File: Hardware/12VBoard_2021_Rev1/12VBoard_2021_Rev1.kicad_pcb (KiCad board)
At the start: 2 copper layers, 178 parts, among them Q1 CSD18537NQ5A, Q2 CSD18531Q5A, Q3 IRFZ34, Q4 CSD18537NQ5A, Q5 CSD18531Q5A, Q6 CSD18537NQ5A, Q7 CSD18531Q5A, SW1 SW_SPDT, U1 LM2576SX-5.0/NOPB, U10 LM5116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

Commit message: fixed H pins x2
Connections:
- net /Tiva In/Outputs/DriveSense renamed Net-(Conn1-Pad1)
- C11 pad 1: /High Current Outputs/Multimedia/Extra/PackVoltage -> /High Current Outputs/PackVoltage
- C14 pad 1: /High Current Outputs/Multimedia/Extra/PackVoltage -> /High Current Outputs/PackVoltage
- C24 pad 1: /High Current Outputs/AuxMount/PackVoltage -> /High Current Outputs/PackVoltage
- C26 pad 1: /High Current Outputs/AuxMount/PackVoltage -> /High Current Outputs/PackVoltage
- C46 pad 1: /High Current Outputs/Multimedia/Extra/PackVoltage -> /High Current Outputs/PackVoltage
- C50 pad 1: /High Current Outputs/AuxMount/PackVoltage -> /High Current Outputs/PackVoltage
- Conn1 pad 3: /Tiva In/Outputs/MulitmediaSense -> /High Current Outputs/MultimediaSense
- R20 pad 1: /High Current Outputs/AuxMount/PackVoltage -> /High Current Outputs/PackVoltage
- R9 pad 1: /High Current Outputs/Multimedia/Extra/PackVoltage -> /High Current Outputs/PackVoltage
- U10 pad 1: /High Current Outputs/AuxMount/PackVoltage -> /High Current Outputs/PackVoltage
- U15 pad 1: /High Current Outputs/Multimedia/Extra/PackVoltage -> /High Current Outputs/PackVoltage
- U17 pad 1: /High Current Outputs/AuxMount/PackVoltage -> /High Current Outputs/PackVoltage
- U7 pad 1: /High Current Outputs/Multimedia/Extra/PackVoltage -> /High Current Outputs/PackVoltage

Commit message: mosfet Net issue: one resolved
the footprint was not updating correctly and had incorrect nets
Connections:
- Q4 pad 1: SW -> /High Current Outputs/PackVoltage
- Q4 pad 2: SW -> /High Current Outputs/PackVoltage
- Q5 pad 2: (no net) -> CS
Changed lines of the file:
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@@
-(kicad_pcb (version 20171130) (host pcbnew "(5.1.5-0)")
+(kicad_pcb (version 20171130) (host pcbnew "(5.1.4)-1")
   (general
     (thickness 1.6)
@@
     (mod_text_size 1 1)
     (mod_text_width 0.15)
-    (pad_size 5.08 5.08)
-    (pad_drill 4.06)
+    (pad_size 4.349999 4.510001)
+    (pad_drill 0)
     (pad_to_mask_clearance 0.05)
     (aux_axis_origin 0 0)
@@
     (pad 3 smd rect (at 0.33 0) (size 4.35 4.51) (layers F.Cu F.Mask)
       (net 47 SW) (solder_paste_margin_ratio -0.5))
-    (pad 1 smd rect (at -2.8 0.635) (size 0.7 0.7) (layers F.Cu F.Paste F.Mask)
-      (net 47 SW) (solder_paste_margin_ratio -0.15))
-    (pad 1 smd rect (at -2.8 -0.635) (size 0.7 0.7) (layers F.Cu F.Paste F.Mask)
-      (net 47 SW) (solder_paste_margin_ratio -0.15))
+    (pad 3 smd rect (at -2.8 0.635) (size 0.7 0.7) (layers F.Cu F.Paste F.Mask)
+      (net 3 "/High Current Outputs/PackVoltage") (solder_paste_margin_ratio -0.15))
+    (pad 2 smd rect (at -2.8 -0.635) (size 0.7 0.7) (layers F.Cu F.Paste F.Mask)
+      (net 3 "/High Current Outputs/PackVoltage") (solder_paste_margin_ratio -0.15))
     (pad 1 smd rect (at -2.8 -1.905) (size 0.7 0.7) (layers F.Cu F.Paste F.Mask)
-      (net 47 SW) (solder_paste_margin_ratio -0.15))
-    (pad 2 smd rect (at -2.8 1.905) (size 0.7 0.7) (layers F.Cu F.Paste F.Mask)
-      (net 47 SW) (solder_paste_margin_ratio -0.15))
+      (net 3 "/High Current Outputs/PackVoltage") (solder_paste_margin_ratio -0.15))
+    (pad 4 smd rect (at -2.8 1.905) (size 0.7 0.7) (layers F.Cu F.Paste F.Mask)
+      (net 48 HO) (solder_paste_margin_ratio -0.15))
     (pad 3 smd rect (at 2.8 1.905) (size 0.7 0.7) (layers F.Cu F.Paste F.Mask)
       (net 47 SW) (solder_paste_margin_ratio -0.15))
@@
       (effects (font (size 1 1) (thickness 0.15)))
     )
-    (pad 3 smd rect (at 2.8 0.635) (size 0.7 0.7) (layers F.Cu F.Paste F.Mask)
-      (net 49 CS) (solder_paste_margin_ratio -0.15))
-    (pad 3 smd rect (at 2.8 -0.635) (size 0.7 0.7) (layers F.Cu F.Paste F.Mask)
-      (net 49 CS) (solder_paste_margin_ratio -0.15))
-    (pad 3 smd rect (at 2.8 -1.905) (size 0.7 0.7) (layers F.Cu F.Paste F.Mask)
-      (net 49 CS) (solder_paste_margin_ratio -0.15))
-    (pad 3 smd rect (at 2.8 1.905) (size 0.7 0.7) (layers F.Cu F.Paste F.Mask)
-      (net 49 CS) (solder_paste_margin_ratio -0.15))
-    (pad 2 smd rect (at -2.8 1.905) (size 0.7 0.7) (layers F.Cu F.Paste F.Mask)
-      (solder_paste_margin_ratio -0.15))
+    (pad 7 smd rect (at 2.8 0.635) (size 0.7 0.7) (layers F.Cu F.Paste F.Mask)
+      (net 47 SW) (solder_paste_margin_ratio -0.15))
+    (pad 6 smd rect (at 2.8 -0.635) (size 0.7 0.7) (layers F.Cu F.Paste F.Mask)
+      (net 47 SW) (solder_paste_margin_ratio -0.15))
+    (pad 5 smd rect (at 2.8 -1.905) (size 0.7 0.7) (layers F.Cu F.Paste F.Mask)
+      (net 47 SW) (solder_paste_margin_ratio -0.15))
+    (pad 8 smd rect (at 2.8 1.905) (size 0.7 0.7) (layers F.Cu F.Paste F.Mask)
+      (net 47 SW) (solder_paste_margin_ratio -0.15))
+    (pad 4 smd rect (at -2.8 1.905) (size 0.7 0.7) (layers F.Cu F.Paste F.Mask)
+      (net 50 LO) (solder_paste_margin_ratio -0.15))
     (pad 1 smd rect (at -2.8 -1.905) (size 0.7 0.7) (layers F.Cu F.Paste F.Mask)
       (net 49 CS) (solder_paste_margin_ratio -0.15))
-    (pad 1 smd rect (at -2.8 -0.635) (size 0.7 0.7) (layers F.Cu F.Paste F.Mask)
+    (pad 2 smd rect (at -2.8 -0.635) (size 0.7 0.7) (layers F.Cu F.Paste F.Mask)
       (net 49 CS) (solder_paste_margin_ratio -0.15))
-    (pad 1 smd rect (at -2.8 0.635) (size 0.7 0.7) (layers F.Cu F.Paste F.Mask)
+    (pad 3 smd rect (at -2.8 0.635) (size 0.7 0.7) (layers F.Cu F.Paste F.Mask)
       (net 49 CS) (solder_paste_margin_ratio -0.15))
-    (pad 3 smd rect (at 0.33 0) (size 4.35 4.51) (layers F.Cu F.Mask)
-      (net 49 CS) (solder_paste_margin_ratio -0.5))
+    (pad 5 smd rect (at 0.33 0) (size 4.349999 4.510001) (layers F.Cu F.Mask)
+      (net 47 SW) (solder_paste_margin_ratio -0.5))
     (pad "" smd rect (at 1.1125 1.095) (size 1.585 1.57) (layers F.Paste))
     (pad "" smd rect (at 1.1125 -1.095) (size 1.585 1.57) (layers F.Paste))

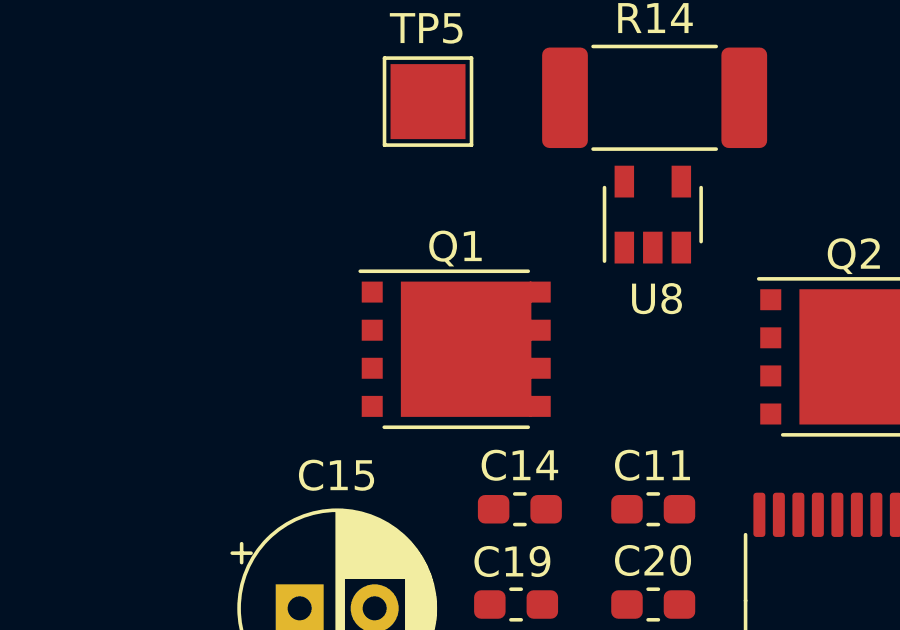
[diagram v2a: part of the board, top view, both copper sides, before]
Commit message: Fixed all nets on Mosfets
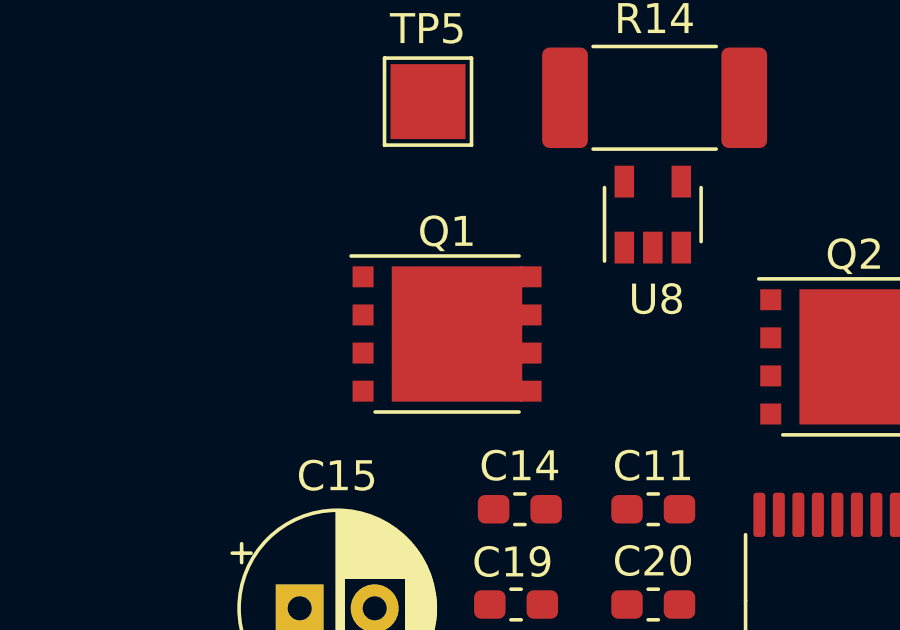
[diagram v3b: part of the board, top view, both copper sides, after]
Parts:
- moved Q1 0.59 mm to (706.8, 54.6)
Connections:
- Q2 pad 2: (no net) -> CS
- Q4 pad 3: SW -> /High Current Outputs/PackVoltage
- Q7 pad 2: (no net) -> CS

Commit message: Finished layout of First high current buck
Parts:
- moved D12 363.9 mm to (359.0, 85.2)
- moved D21 363.9 mm to (361.8, 116.0)
- moved D23 363.9 mm to (385.3, 117.6)
- moved Q2 363.9 mm to (356.6, 66.4)
- moved Q7 363.9 mm to (383.3, 66.7)
- moved TP7 363.9 mm to (370.1, 58.0)
- moved TP9 363.9 mm to (343.8, 103.5)
- moved U8 363.9 mm to (349.9, 61.7)
- moved C12 363.9 mm to (354.3, 85.0)
- moved C14 363.9 mm to (345.5, 71.5)
- moved C15 363.9 mm to (338.1, 74.8)
- moved C18 363.9 mm to (338.1, 83.4)
- moved C34 363.9 mm to (372.9, 71.8)
- moved C36 363.9 mm to (377.2, 71.8)
- moved C37 363.9 mm to (365.6, 84.2)
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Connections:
- Q4 pad 1: /High Current Outputs/PackVoltage -> SW
- Q4 pad 2: /High Current Outputs/PackVoltage -> SW
- Q4 pad 3: /High Current Outputs/PackVoltage -> SW
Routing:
- net HO: track 0.00 -> 9.89 mm, vias 0 -> 2
- net SW: track 0.00 -> 6.01 mm
- added copper zone on F.Cu, net SW
- added copper zone on F.Cu, net VOUTVCCX

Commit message: First Buck Arranged
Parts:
- removed C25: 1uF, Capacitor_SMD:C_0603_1608Metric_Pad1.05x0.95mm_HandSolder
- C29, C31, C32, D15, R19, R21, R22, R23, U10, U12, U7: moved to B.Cu
- moved TP7 303.8 mm to (66.3, 54.1)
- moved TP5 271.9 mm to (70.7, 47.1)
- moved C13 221.1 mm to (124.5, 92.3)
- moved C16 221.1 mm to (124.5, 89.0)
- moved C17 221.1 mm to (129.0, 89.0)
- moved C19 221.1 mm to (124.5, 85.5)
- moved C20 221.1 mm to (129.0, 85.5)
- moved R10 221.1 mm to (124.6, 95.8)
- moved R11 221.1 mm to (124.6, 99.2)
- moved R12 221.1 mm to (129.0, 99.2)
- moved R13 221.1 mm to (129.0, 92.3)
- moved R8 221.1 mm to (133.6, 99.2)
- moved R9 221.1 mm to (129.0, 95.8)
- moved C12 221.1 mm to (133.5, 95.8)
- moved D12 221.1 mm to (138.2, 96.0)
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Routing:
- net Net-(SW1-Pad2): track 0.00 -> 46.2 mm, vias 0 -> 1
- net /High Current Outputs/AuxCTL: track 0.00 -> 41.2 mm, vias 0 -> 2
- net VOUTVCCX: track 0.00 -> 28.2 mm, vias 0 -> 3
- net CS: track 0.00 -> 19.3 mm, vias 0 -> 1
- net /High Current Outputs/5V: track 40.9 -> 21.8 mm
- net /High Current Outputs/PackVoltage: track 55.0 -> 67.0 mm, vias 13 -> 14
- net /Low Current Outputs/CurrentSense: track 55.1 -> 43.1 mm
- net Net-(R20-Pad2): track 0.00 -> 11.8 mm, vias 0 -> 1
- net LO: track 0.00 -> 11.4 mm, vias 0 -> 1
- net COMPFB: track 0.00 -> 9.18 mm, vias 0 -> 3
- net VCC: track 0.00 -> 9.08 mm, vias 0 -> 2
- net /High Current Outputs/Multimedia/Extra/12V10AMultimedia: track 0.00 -> 8.63 mm, vias 0 -> 1
- net Net-(C31-Pad1): track 0.00 -> 8.01 mm
- net HB: track 0.00 -> 7.45 mm, vias 0 -> 1
- net Net-(C32-Pad1): track 0.00 -> 6.70 mm
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- added copper zone on B.Cu, net /High Current Outputs/Gimbal/12V5AGimbal
- added copper zone on F.Cu, net /High Current Outputs/Gimbal/12V5AGimbal
- added copper zone on B.Cu, net /High Current Outputs/Multimedia/Extra/12V10AExtra
- added copper zone on F.Cu, net /High Current Outputs/Multimedia/Extra/12V10AExtra
- added copper zone on B.Cu, net /High Current Outputs/Multimedia/Extra/12V10AMultimedia
- added copper zone on F.Cu, net /High Current Outputs/Multimedia/Extra/12V10AMultimedia
- added copper zone on B.Cu, net Net-(Q3-Pad2)
- added copper zone on F.Cu, net Net-(Q3-Pad2)
- removed copper zone on F.Cu, net Net-(C10-Pad1)
- removed copper zone on B.Cu, net Net-(F2-Pad2)

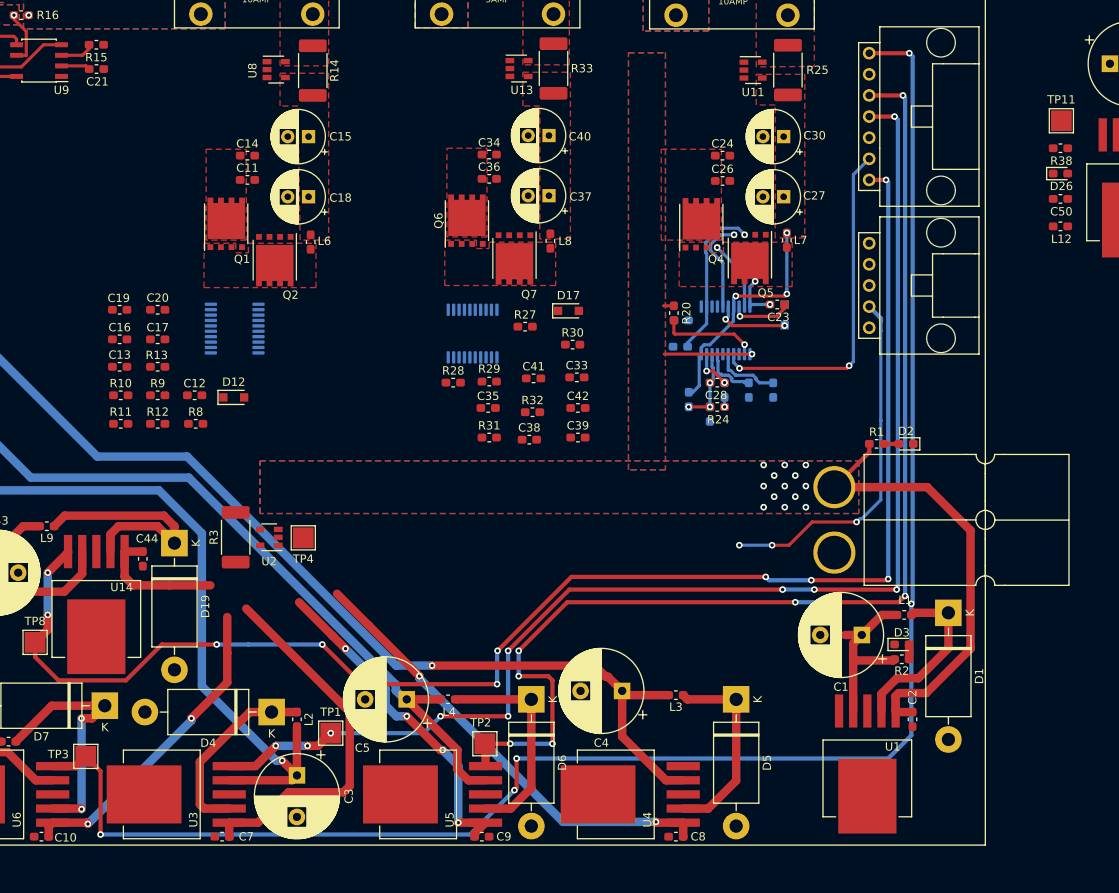
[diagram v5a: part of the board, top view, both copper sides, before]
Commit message: Re arranged bucks for more space
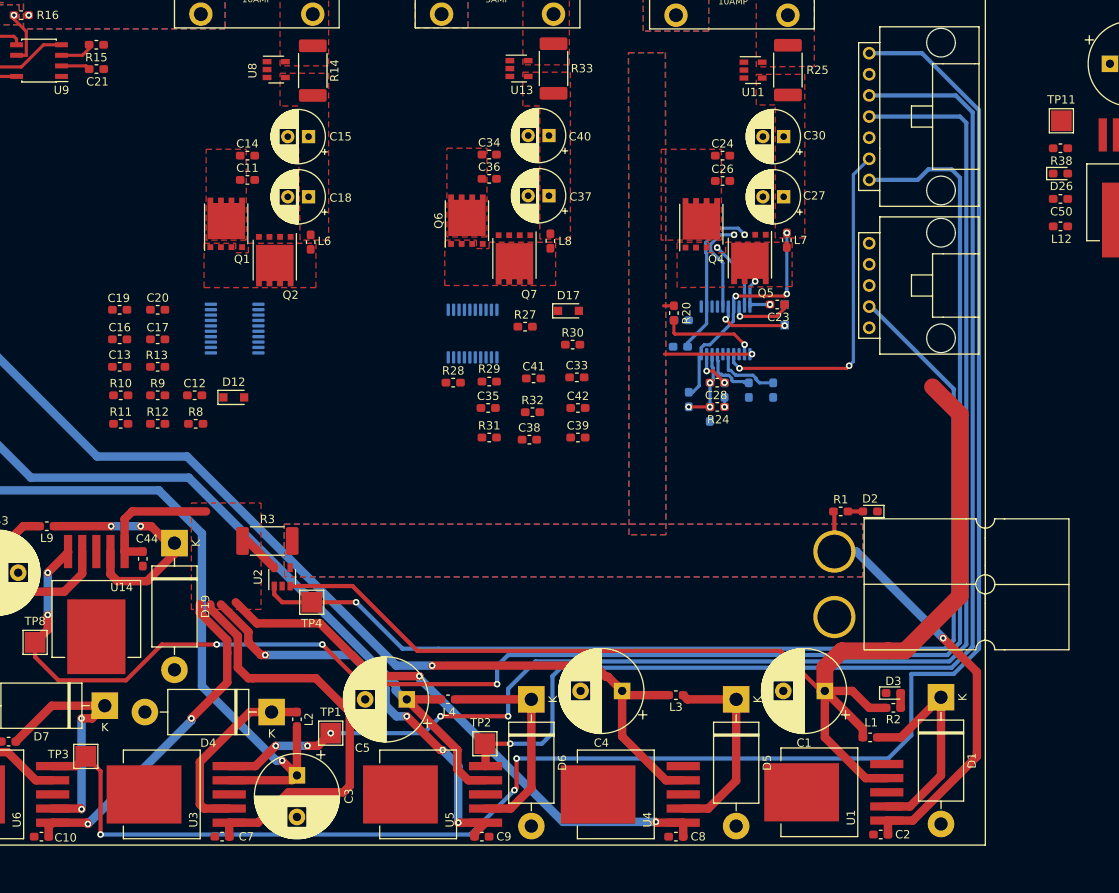
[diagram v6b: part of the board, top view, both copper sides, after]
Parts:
- moved L1 15.3 mm to (214.7, 136.9)
- moved C2 14.4 mm to (216.0, 148.6), turned to 180 degrees
- moved D1 10.2 mm to (223.3, 132.1)
- moved D2 9.20 mm to (214.7, 109.7)
- moved R1 9.20 mm to (211.2, 109.7)
- moved C1 8.07 mm to (209.3, 131.3)
- moved TP4 7.81 mm to (147.6, 120.7)
- moved Conn3 7.75 mm to (210.5, 122.4)
- moved D3 5.93 mm to (217.5, 131.6)
- moved R2 5.93 mm to (217.5, 133.3)
- moved U1 5.28 mm to (210.4, 143.5), turned to 90 degrees
- moved U2 5.01 mm to (144.0, 117.6), turned to 90 degrees
- moved R3 3.84 mm to (142.2, 113.3), turned to 0 degrees
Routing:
- net /High Current Outputs/5V: track 21.8 -> 149.4 mm
- net /Low Current Outputs/CurrentSense: track 43.1 -> 130.3 mm, vias 3 -> 1
- net Net-(C10-Pad1): track 194.2 -> 231.4 mm
- net /Low Current Outputs/DriveCTL: track 179.9 -> 201.6 mm, vias 10 -> 5
- net /Tiva In/Outputs/CameraCTL: track 153.9 -> 171.4 mm, vias 10 -> 5
- net /Tiva In/Outputs/ExtraCTL: track 206.3 -> 216.8 mm, vias 5 -> 3
- net /Tiva In/Outputs/NavBoardCTL: track 139.4 -> 147.8 mm, vias 8 -> 1
- net Net-(D1-Pad1): track 21.2 -> 27.1 mm
- net /High Current Outputs/PackVoltage: track 67.0 -> 66.0 mm, vias 14 -> 2
- net Net-(D19-Pad1): track 28.6 -> 28.7 mm, vias 0 -> 2
- added copper zone on F.Cu, net Net-(C10-Pad1)

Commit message: Lunch Break
Routing thinzs
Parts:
- added C25: 1uF, Capacitor_SMD:C_0603_1608Metric_Pad1.05x0.95mm_HandSolder, F.Cu at (394.2, 99.8)
- D21, D23, D25: footprint Diode_THT:D_DO-201AD_P15.24mm_Horizontal -> Diode_THT:D_DO-201AD_P5.08mm_Vertical_KathodeUp
- U17: moved to B.Cu
- moved U17 43.8 mm to (215.2, 101.7), turned to 90 degrees
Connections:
- Q1 pad 4: LO -> HO
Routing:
- net /High Current Outputs/5V: track 149.4 -> 352.0 mm
- net /High Current Outputs/Multimedia/Extra/12V10AMultimedia: track 8.63 -> 17.0 mm, vias 1 -> 2
- net /High Current Outputs/AuxCTL: track 41.2 -> 39.5 mm

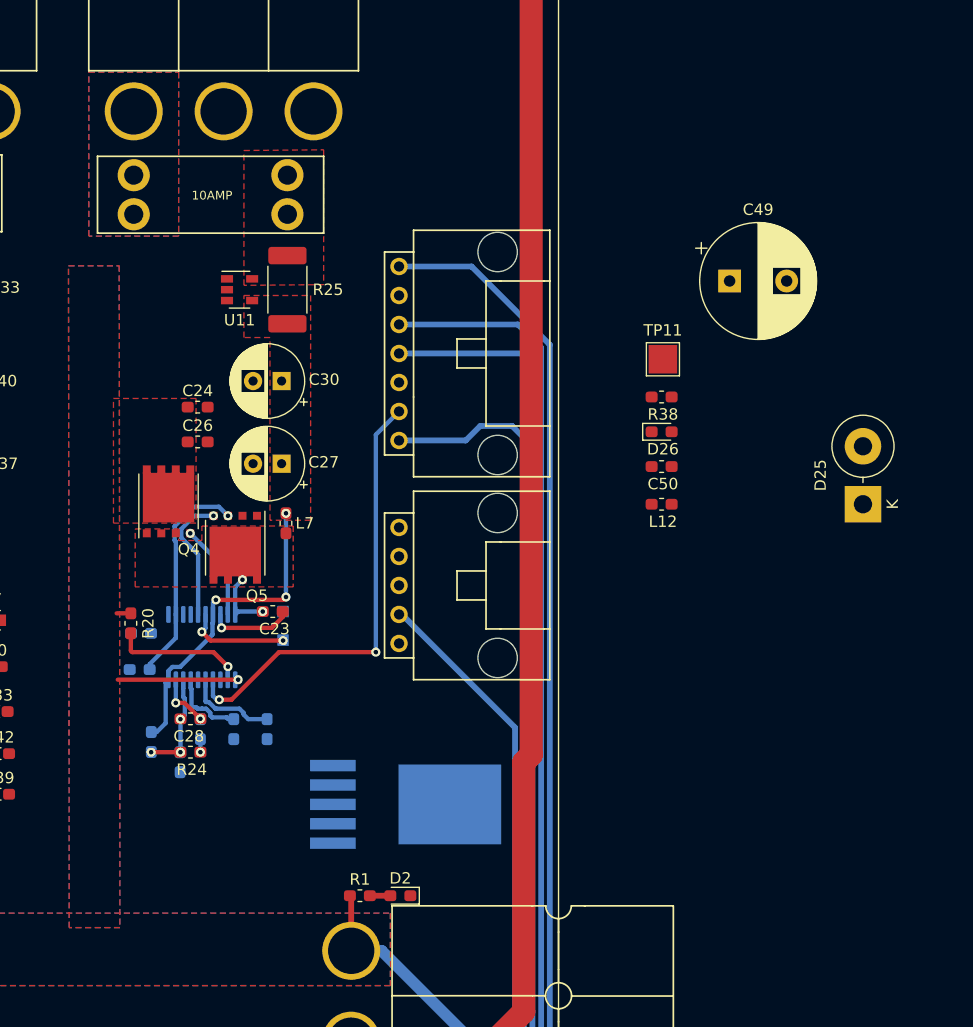
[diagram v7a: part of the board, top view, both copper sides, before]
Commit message: Finished first full high side layout
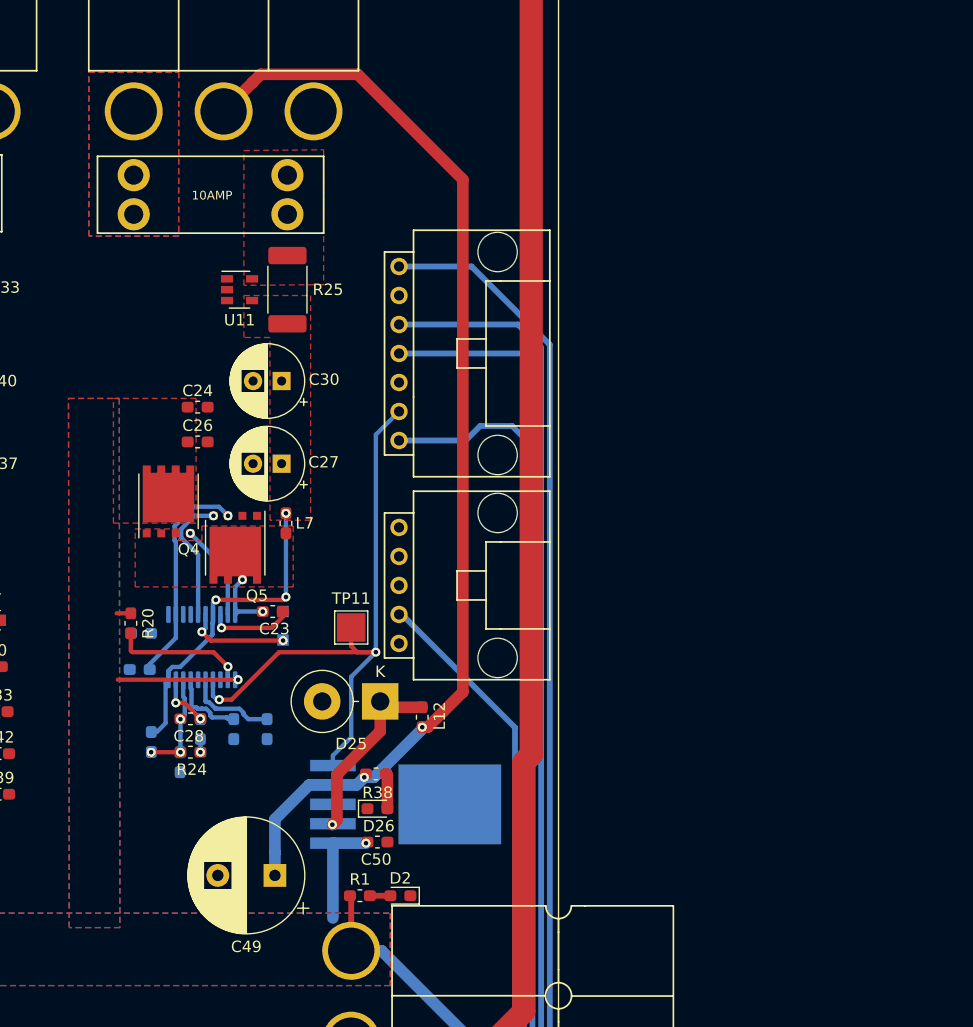
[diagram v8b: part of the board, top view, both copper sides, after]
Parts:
- moved C49 65.6 mm to (203.8, 108.0), turned to 180 degrees
- moved D25 45.7 mm to (213.0, 92.7), turned to 180 degrees
- moved R38 41.4 mm to (212.6, 99.1), turned to 0 degrees
- moved D26 41.4 mm to (212.7, 102.1)
- moved C50 41.2 mm to (212.7, 105.0), turned to 0 degrees
- moved TP11 36.0 mm to (210.4, 86.2)
- moved L12 28.1 mm to (216.7, 94.1), turned to 270 degrees
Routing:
- net /High Current Outputs/AuxMount/12V3AAuxMountLogic: track 0.00 -> 97.1 mm, vias 0 -> 2
- net Net-(D25-Pad1): track 0.00 -> 16.5 mm, vias 0 -> 1
- net /High Current Outputs/AuxCTL: track 39.5 -> 55.0 mm
- net /High Current Outputs/PackVoltage: track 66.0 -> 75.5 mm, vias 2 -> 3
- net Net-(D26-Pad2): track 0.00 -> 3.10 mm
